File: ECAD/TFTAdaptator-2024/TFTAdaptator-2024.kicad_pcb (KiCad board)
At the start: 2 copper layers, 26 x 28 mm, 2 parts, among them J1 Conn_01x09

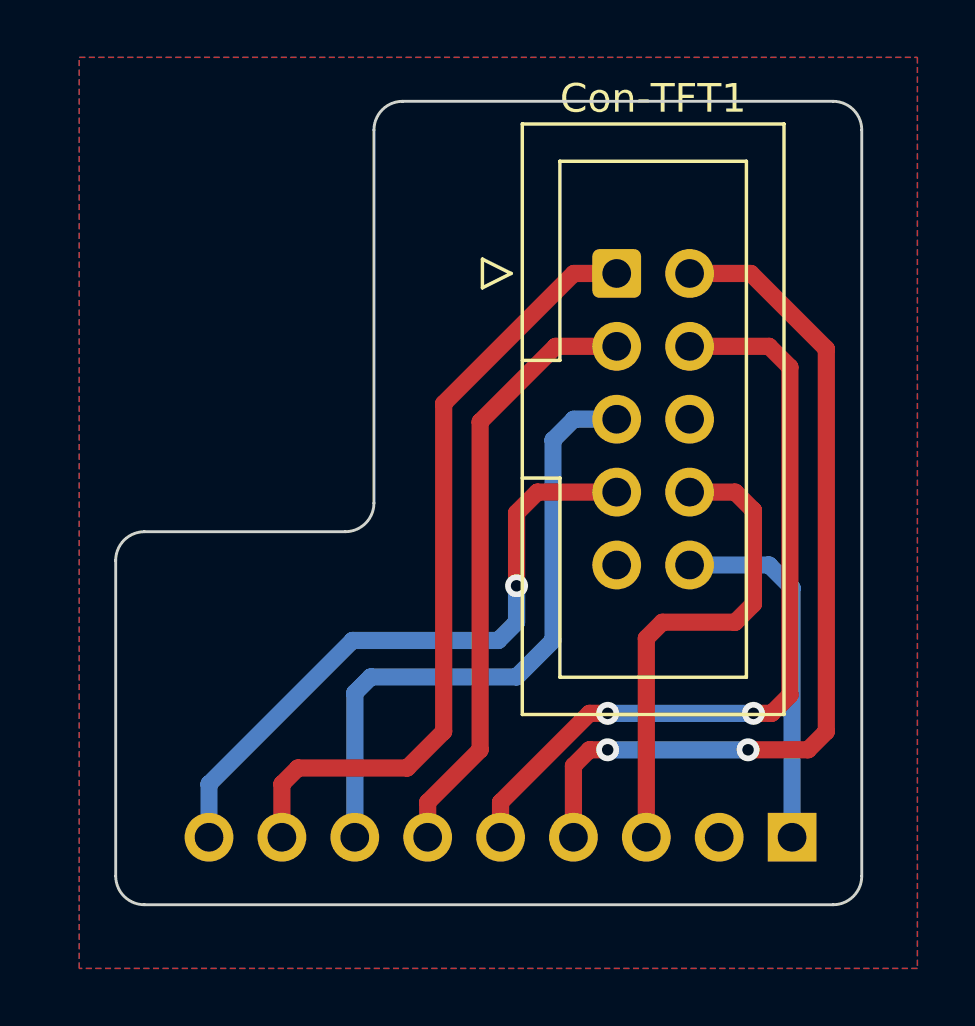
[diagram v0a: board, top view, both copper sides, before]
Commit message: update silkscreen, dimensions and DRC
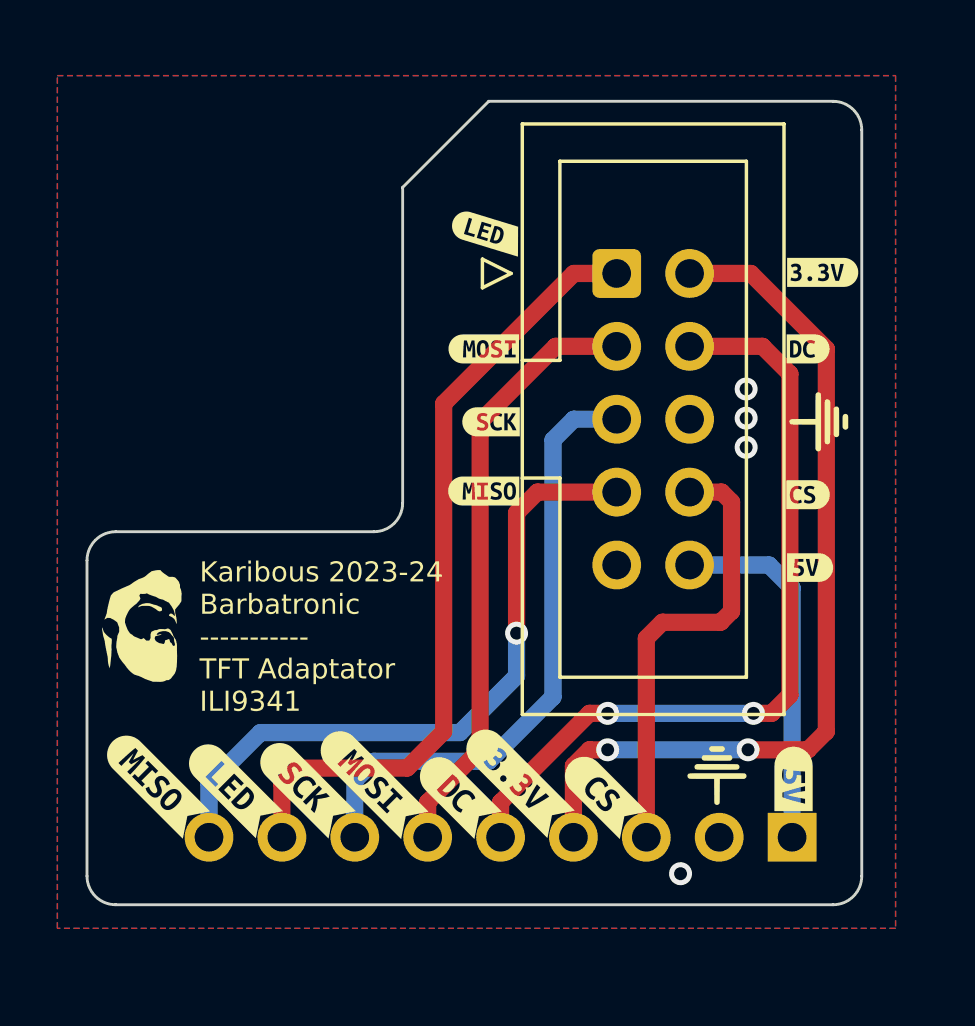
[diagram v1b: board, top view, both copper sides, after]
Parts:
- added G***: LOGO, LOGO, F.Cu at (127.9, 97.3)
- added G***: LOGO, LOGO, F.Cu at (151.5, 90.2)
- added G***: LOGO, LOGO, F.Cu at (148.0, 102.5)
- added kibuzzard-64933136: G***, kibuzzard-64933136, F.Cu at (141.0, 102.6)
- added kibuzzard-64E9C866: G***, kibuzzard-64E9C866, F.Cu at (143.9, 103.1)
- added kibuzzard-64E9C890: G***, kibuzzard-64E9C890, F.Cu at (138.9, 103.1)
- added kibuzzard-64E9C897: G***, kibuzzard-64E9C897, F.Cu at (135.9, 102.7)
- added kibuzzard-64E9C89C: G***, kibuzzard-64E9C89C, F.Cu at (133.6, 102.9)
- added kibuzzard-64E9C8A2: G***, kibuzzard-64E9C8A2, F.Cu at (131.1, 102.9)
- added kibuzzard-64E9CBF9: G***, kibuzzard-64E9CBF9, F.Cu at (150.6, 102.6)
- added kibuzzard-64E9CDB6: G***, kibuzzard-64E9CDB6, F.Cu at (151.1, 87.6)
- added kibuzzard-64E9CDBF: G***, kibuzzard-64E9CDBF, F.Cu at (151.1, 92.7)
- added kibuzzard-64E9CDD4: G***, kibuzzard-64E9CDD4, F.Cu at (151.6, 85.0)
- added kibuzzard-64E9CDE3: G***, kibuzzard-64E9CDE3, F.Cu at (151.2, 95.2)
- added kibuzzard-64E9CE87: G***, kibuzzard-64E9CE87, F.Cu at (139.8, 87.6)
- added kibuzzard-64E9CE8E: G***, kibuzzard-64E9CE8E, F.Cu at (140.1, 90.2)
- added kibuzzard-64E9CE93: G***, kibuzzard-64E9CE93, F.Cu at (139.8, 92.6)
- added kibuzzard-64E9CEBE: G***, kibuzzard-64E9CEBE, F.Cu at (140.0, 83.6)
- added kibuzzard-64E9CFC9: G***, kibuzzard-64E9CFC9, F.Cu at (128.4, 102.8)
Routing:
- net TFT_CS: track 16.9 -> 15.7 mm
- net TFT_MISO: track 22.5 -> 23.6 mm
- net TFT_SCK: track 22.2 -> 21.6 mm
- net GND: vias 0 -> 4
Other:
- board size 26 x 28 mm -> 27 x 28 mm
- board text added: "Karibous 2023-24 Barbatronic ----------- TFT Adaptator ILI9341"
